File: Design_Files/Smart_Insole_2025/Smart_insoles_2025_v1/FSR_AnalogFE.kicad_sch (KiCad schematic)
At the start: 33 parts, among them J1 Conn_01x20, U8 MCP6004-I_ST, U9 MCP6004-I_ST

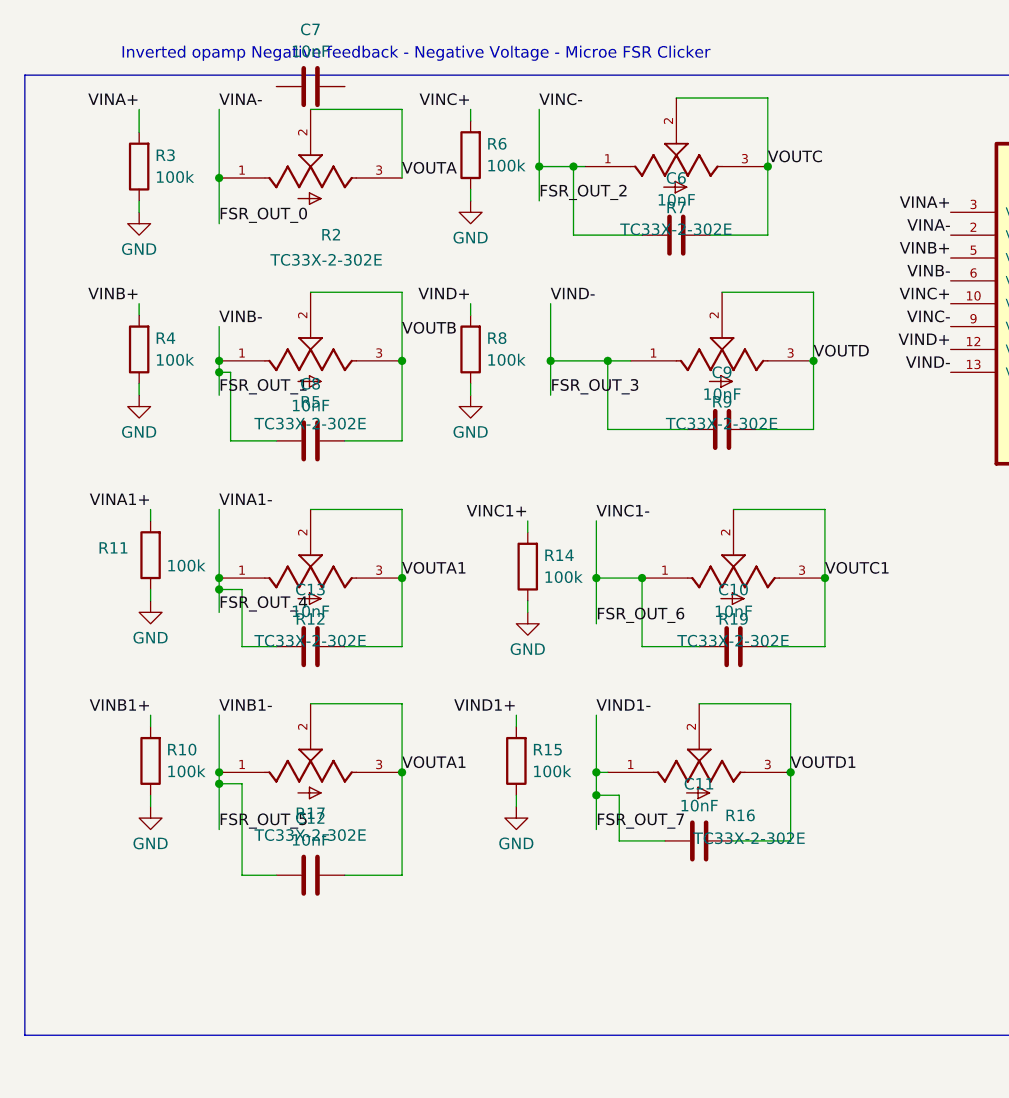
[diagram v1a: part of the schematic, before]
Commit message: Added battery connector footprint. Grouping componnets in PcbNew
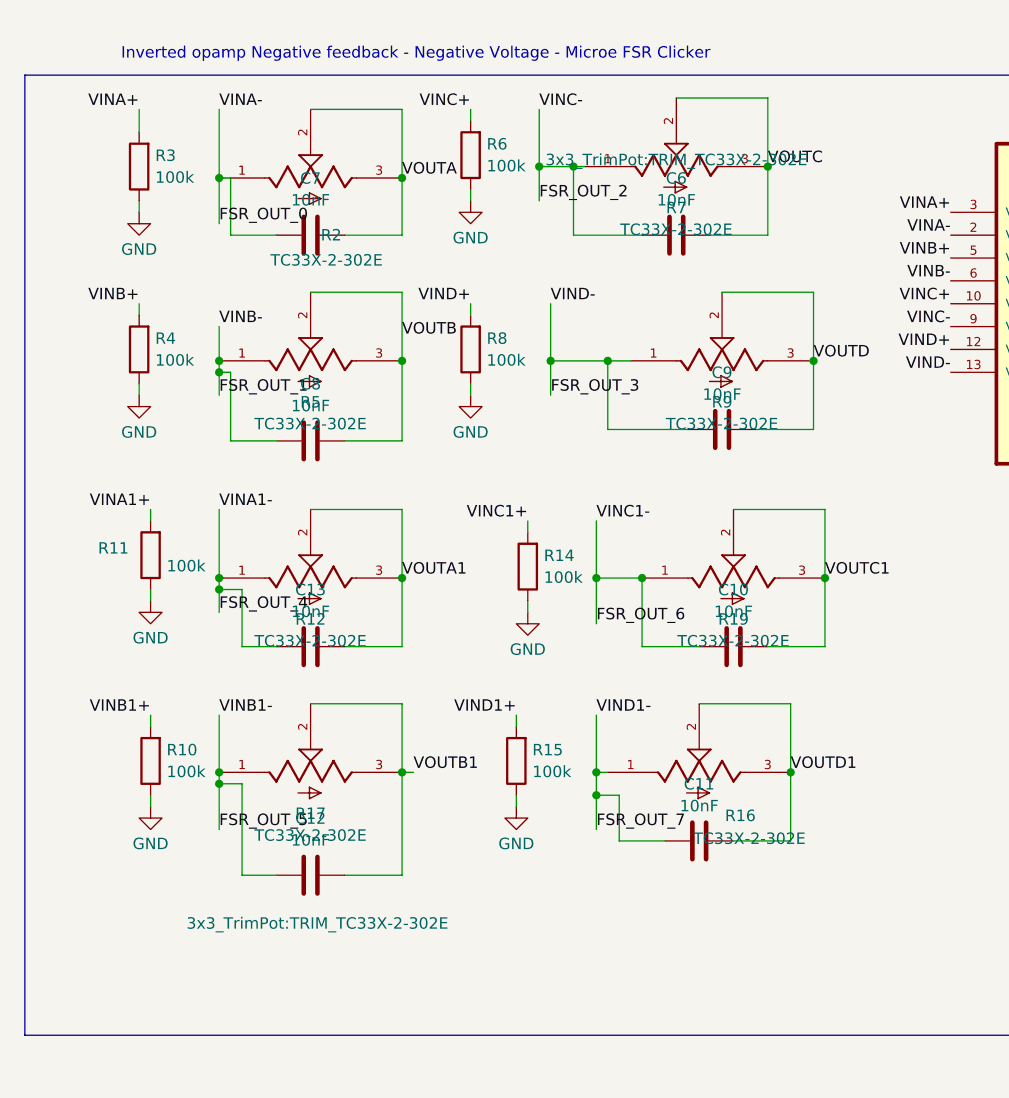
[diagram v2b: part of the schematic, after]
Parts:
- R12, R16, R17, R19, R2, R5, R7, R9: footprint TC33X-2-302E:TRIM_TC33X-2-302E -> 3x3_TrimPot:TRIM_TC33X-2-302E
- U9: footprint MCP6004-I_ST:SOP65P640X120-14N -> MCP6004_I_ST:SOP65P640X120-14N
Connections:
- net FSR_OUT_0: now also C7.1
- net VOUTA: now also C7.2
- net VOUTA1: no longer C12.2, R17.2, R17.3
- net VOUTB1: now also C12.2, R17.2, R17.3
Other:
- moved on the sheet: C7
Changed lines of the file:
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@@
 	)
 	(junction
+		(at 67.31 30.48)
+		(diameter 0)
+		(color 0 0 0 0)
+	)
+	(junction
 		(at 88.9 96.52)
 		(diameter 0)
@@
 	(wire
 		(pts
+			(xy 48.26 30.48) (xy 46.99 30.48)
+		)
+		(stroke
+			(width 0)
+			(type default)
+		)
+	)
+	(wire
+		(pts
 			(xy 86.36 29.21) (xy 87.63 29.21)
 		)
@@
 	(wire
 		(pts
+			(xy 60.96 36.83) (xy 67.31 36.83)
+		)
+		(stroke
+			(width 0)
+			(type default)
+		)
+	)
+	(wire
+		(pts
 			(xy 181.61 29.21) (xy 163.83 29.21)
 		)
@@
 	(wire
 		(pts
+			(xy 68.58 96.52) (xy 67.31 96.52)
+		)
+		(stroke
+			(width 0)
+			(type default)
+		)
+	)
+	(wire
+		(pts
 			(xy 86.36 36.83) (xy 93.98 36.83)
 		)
@@
 	(wire
 		(pts
+			(xy 53.34 36.83) (xy 48.26 36.83)
+		)
+		(stroke
+			(width 0)
+			(type default)
+		)
+	)
+	(wire
+		(pts
 			(xy 83.82 44.45) (xy 83.82 50.8)
 		)
@@
 	(wire
 		(pts
+			(xy 67.31 36.83) (xy 67.31 30.48)
+		)
+		(stroke
+			(width 0)
+			(type default)
+		)
+	)
+	(wire
+		(pts
 			(xy 67.31 88.9) (xy 67.31 96.52)
 		)
@@
 	(wire
 		(pts
+			(xy 48.26 36.83) (xy 48.26 30.48)
+		)
+		(stroke
+			(width 0)
+			(type default)
+		)
+	)
+	(wire
+		(pts
 			(xy 83.82 50.8) (xy 83.82 54.61)
 		)
@@
 		)
 	)
-	(label "VOUTA1"
-		(at 67.31 96.52 0)
+	(label "VOUTB1"
+		(at 68.58 96.52 0)
 		(fields_autoplaced yes)
 		(effects
@@
 			)
 		)
-		(property "Footprint" "TC33X-2-302E:TRIM_TC33X-2-302E"
+		(property "Footprint" "3x3_TrimPot:TRIM_TC33X-2-302E"
 			(at 97.79 29.21 0)
 			(effects
@@
 				)
 				(justify bottom)
-				(hide yes)
 			)
 		)
@@
 			)
 		)
-		(property "Footprint" "TC33X-2-302E:TRIM_TC33X-2-302E"
+		(property "Footprint" "3x3_TrimPot:TRIM_TC33X-2-302E"
 			(at 57.15 74.93 0)
 			(effects
@@
 	(symbol
 		(lib_id "Device:C")
-		(at 57.15 20.32 90)
+		(at 57.15 36.83 90)
 		(unit 1)
 		(exclude_from_sim no)
@@
 		(fields_autoplaced yes)
 		(property "Reference" "C7"
-			(at 57.15 14.0165 90)
+			(at 57.15 30.5265 90)
 			(effects
 				(font
@@
 		)
 		(property "Value" "10nF"
-			(at 57.15 16.4408 90)
+			(at 57.15 32.9508 90)
 			(effects
 				(font
@@
 		)
 		(property "Footprint" "Capacitor_SMD:C_0603_1608Metric_Pad1.08x0.95mm_HandSolder"
-			(at 60.96 19.3548 0)
+			(at 60.96 35.8648 0)
 			(effects
 				(font
@@
 		)
 		(property "Datasheet" "~"
-			(at 57.15 20.32 0)
+			(at 57.15 36.83 0)
 			(effects
 				(font
@@
 		)
 		(property "Description" "Unpolarized capacitor"
-			(at 57.15 20.32 0)
+			(at 57.15 36.83 0)
 			(effects
 				(font
@@
 			)
 		)
-		(property "Footprint" "TC33X-2-302E:TRIM_TC33X-2-302E"
+		(property "Footprint" "3x3_TrimPot:TRIM_TC33X-2-302E"
 			(at 100.33 96.52 0)
 			(effects
@@
 			)
 		)
-		(property "Footprint" "MCP6004-I_ST:SOP65P640X120-14N"
+		(property "Footprint" "MCP6004_I_ST:SOP65P640X120-14N"
 			(at 233.68 44.45 0)
 			(effects
@@
 			)
 		)
-		(property "Footprint" "TC33X-2-302E:TRIM_TC33X-2-302E"
+		(property "Footprint" "3x3_TrimPot:TRIM_TC33X-2-302E"
 			(at 102.87 50.8 0)
 			(effects
@@
 			)
 		)
-		(property "Footprint" "TC33X-2-302E:TRIM_TC33X-2-302E"
+		(property "Footprint" "3x3_TrimPot:TRIM_TC33X-2-302E"
 			(at 57.15 30.48 0)
 			(effects
@@
 			)
 		)
-		(property "Footprint" "TC33X-2-302E:TRIM_TC33X-2-302E"
+		(property "Footprint" "3x3_TrimPot:TRIM_TC33X-2-302E"
 			(at 57.15 50.8 0)
 			(effects
@@
 		(on_board yes)
 		(dnp no)
-		(fields_autoplaced yes)
 		(property "Reference" "R17"
 			(at 57.15 101.1103 0)
@@
 			)
 		)
-		(property "Footprint" "TC33X-2-302E:TRIM_TC33X-2-302E"
-			(at 57.15 96.52 0)
+		(property "Footprint" "3x3_TrimPot:TRIM_TC33X-2-302E"
+			(at 57.912 114.046 0)
 			(effects
 				(font
@@
 				)
 				(justify bottom)
-				(hide yes)
 			)
 		)
@@
 			)
 		)
-		(property "Footprint" "TC33X-2-302E:TRIM_TC33X-2-302E"
+		(property "Footprint" "3x3_TrimPot:TRIM_TC33X-2-302E"
 			(at 104.14 74.93 0)
 			(effects

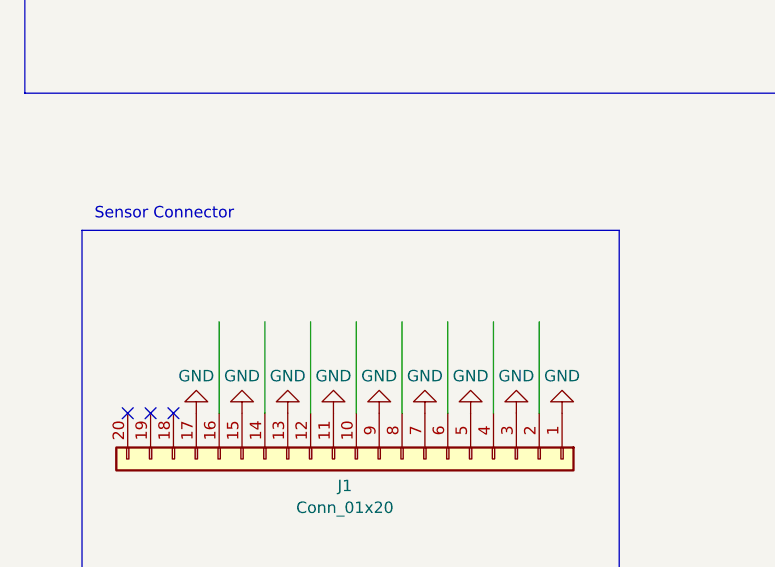
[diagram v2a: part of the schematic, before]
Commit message: PCBnew:Moving placed components. Fixed REF of mcp component
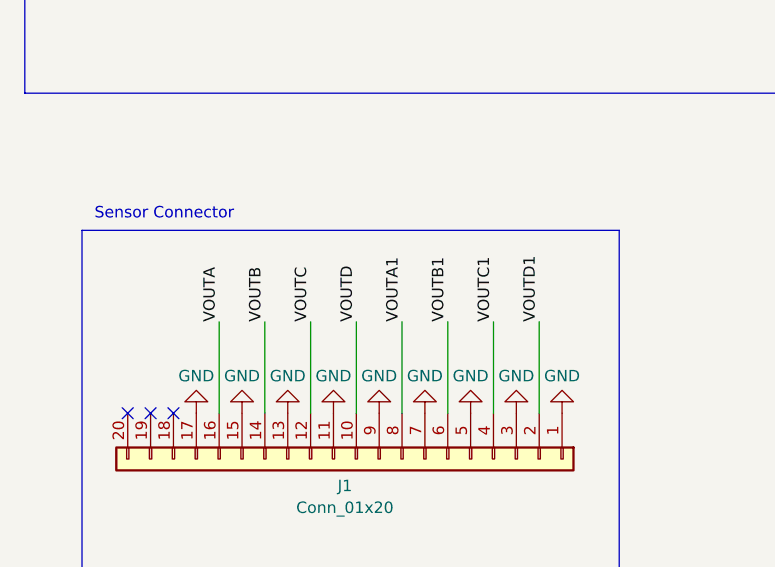
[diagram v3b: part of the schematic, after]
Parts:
- U8, U9: footprint MCP6004_I_ST:SOP65P640X120-14N -> MCP6004_I_ST:custom
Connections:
- net VOUTA: now also J1.16 (Pin_16)
- net VOUTA1: now also J1.8 (Pin_8)
- net VOUTB: now also J1.14 (Pin_14)
- net VOUTB1: now also J1.6 (Pin_6)
- net VOUTC: now also J1.12 (Pin_12)
- net VOUTC1: now also J1.4 (Pin_4)
- net VOUTD: now also J1.10 (Pin_10)
- net VOUTD1: now also J1.2 (Pin_2)
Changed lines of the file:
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@@
 	(wire
 		(pts
-			(xy 72.39 151.13) (xy 72.39 161.29)
-		)
-		(stroke
-			(width 0)
-			(type default)
-		)
-	)
-	(wire
-		(pts
 			(xy 86.36 36.83) (xy 86.36 29.21)
 		)
@@
 	(wire
 		(pts
+			(xy 72.39 151.13) (xy 72.39 161.29)
+		)
+		(stroke
+			(width 0)
+			(type default)
+		)
+	)
+	(wire
+		(pts
 			(xy 39.37 99.06) (xy 39.37 100.33)
 		)
@@
 		)
 	)
+	(label "VOUTA"
+		(at 46.99 151.13 90)
+		(fields_autoplaced yes)
+		(effects
+			(font
+				(size 1.27 1.27)
+			)
+			(justify left bottom)
+		)
+	)
 	(label "FSR_OUT_0"
 		(at 46.99 35.56 0)
@@
 		)
 	)
+	(label "VOUTD"
+		(at 62.23 151.13 90)
+		(fields_autoplaced yes)
+		(effects
+			(font
+				(size 1.27 1.27)
+			)
+			(justify left bottom)
+		)
+	)
 	(label "VIND+"
 		(at 74.93 44.45 180)
@@
 		)
 	)
+	(label "VOUTA1"
+		(at 67.31 151.13 90)
+		(fields_autoplaced yes)
+		(effects
+			(font
+				(size 1.27 1.27)
+			)
+			(justify left bottom)
+		)
+	)
 	(label "VINC1+"
 		(at 81.28 68.58 180)
@@
 		)
 	)
+	(label "VOUTB1"
+		(at 72.39 151.13 90)
+		(fields_autoplaced yes)
+		(effects
+			(font
+				(size 1.27 1.27)
+			)
+			(justify left bottom)
+		)
+	)
 	(label "VOUTA"
 		(at 67.31 30.48 0)
@@
 		)
 	)
+	(label "VOUTC"
+		(at 57.15 151.13 90)
+		(fields_autoplaced yes)
+		(effects
+			(font
+				(size 1.27 1.27)
+			)
+			(justify left bottom)
+		)
+	)
 	(label "VINB-"
 		(at 46.99 46.99 0)
@@
 		)
 	)
+	(label "VOUTB"
+		(at 52.07 151.13 90)
+		(fields_autoplaced yes)
+		(effects
+			(font
+				(size 1.27 1.27)
+			)
+			(justify left bottom)
+		)
+	)
 	(label "VINA-"
 		(at 46.99 22.86 0)
@@
 		)
 	)
+	(label "VOUTD1"
+		(at 82.55 151.13 90)
+		(fields_autoplaced yes)
+		(effects
+			(font
+				(size 1.27 1.27)
+			)
+			(justify left bottom)
+		)
+	)
 	(label "VINB1-"
 		(at 46.99 90.17 0)
@@
 		)
 	)
+	(label "VOUTC1"
+		(at 77.47 151.13 90)
+		(fields_autoplaced yes)
+		(effects
+			(font
+				(size 1.27 1.27)
+			)
+			(justify left bottom)
+		)
+	)
 	(label "VOUTB1"
 		(at 68.58 96.52 0)
@@
 			)
 		)
-		(property "Footprint" "MCP6004_I_ST:SOP65P640X120-14N"
+		(property "Footprint" "MCP6004_I_ST:custom"
 			(at 146.05 44.45 0)
 			(effects
@@
 			)
 		)
+		(property "MPN" ""
+			(at 146.05 44.45 0)
+			(effects
+				(font
+					(size 1.27 1.27)
+				)
+			)
+		)
+		(property "Manufacturer" ""
+			(at 146.05 44.45 0)
+			(effects
+				(font
+					(size 1.27 1.27)
+				)
+			)
+		)
+		(property "3D model" ""
+			(at 146.05 44.45 0)
+			(effects
+				(font
+					(size 1.27 1.27)
+				)
+			)
+		)
+		(property "Notes" ""
+			(at 146.05 44.45 0)
+			(effects
+				(font
+					(size 1.27 1.27)
+				)
+			)
+		)
+		(property "LCSC Part #" ""
+			(at 146.05 44.45 0)
+			(effects
+				(font
+					(size 1.27 1.27)
+				)
+			)
+		)
+		(property "LCSC MPN" ""
+			(at 146.05 44.45 0)
+			(effects
+				(font
+					(size 1.27 1.27)
+				)
+			)
+		)
+		(property "LCSC Manufacturer" ""
+			(at 146.05 44.45 0)
+			(effects
+				(font
+					(size 1.27 1.27)
+				)
+			)
+		)
 		(pin "1"
 		)
@@
 			)
 		)
-		(property "Footprint" "MCP6004_I_ST:SOP65P640X120-14N"
+		(property "Footprint" "MCP6004_I_ST:custom"
 			(at 233.68 44.45 0)
 			(effects
@@
 			)
 		)
+		(property "MPN" ""
+			(at 233.68 44.45 0)
+			(effects
+				(font
+					(size 1.27 1.27)
+				)
+			)
+		)
+		(property "Manufacturer" ""
+			(at 233.68 44.45 0)
+			(effects
+				(font
+					(size 1.27 1.27)
+				)
+			)
+		)
+		(property "3D model" ""
+			(at 233.68 44.45 0)
+			(effects
+				(font
+					(size 1.27 1.27)
+				)
+			)
+		)
+		(property "Notes" ""
+			(at 233.68 44.45 0)
+			(effects
+				(font
+					(size 1.27 1.27)
+				)
+			)
+		)
+		(property "LCSC Part #" ""
+			(at 233.68 44.45 0)
+			(effects
+				(font
+					(size 1.27 1.27)
+				)
+			)
+		)
+		(property "LCSC MPN" ""
+			(at 233.68 44.45 0)
+			(effects
+				(font
+					(size 1.27 1.27)
+				)
+			)
+		)
+		(property "LCSC Manufacturer" ""
+			(at 233.68 44.45 0)
+			(effects
+				(font
+					(size 1.27 1.27)
+				)
+			)
+		)

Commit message: PCB new moving things around
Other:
- moved on the sheet: C17
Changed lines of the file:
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@@
 	)
 	(junction
-		(at 264.16 27.94)
+		(at 264.16 29.21)
 		(diameter 0)
 		(color 0 0 0 0)
@@
 	(wire
 		(pts
-			(xy 251.46 29.21) (xy 251.46 27.94)
-		)
-		(stroke
-			(width 0)
-			(type default)
-		)
-	)
-	(wire
-		(pts
 			(xy 67.31 151.13) (xy 67.31 161.29)
 		)
@@
 	(wire
 		(pts
-			(xy 251.46 27.94) (xy 264.16 27.94)
+			(xy 251.46 29.21) (xy 264.16 29.21)
 		)
 		(stroke
@@
 	(symbol
 		(lib_id "power:VCC")
-		(at 264.16 27.94 0)
+		(at 264.16 29.21 0)
 		(unit 1)
 		(exclude_from_sim no)
@@
 		(fields_autoplaced yes)
 		(property "Reference" "#PWR045"
-			(at 264.16 31.75 0)
+			(at 264.16 33.02 0)
 			(effects
 				(font
@@
 		)
 		(property "Value" "VCC"
-			(at 264.16 23.8069 0)
+			(at 264.16 25.0769 0)
 			(effects
 				(font
@@
 		)
 		(property "Footprint" ""
-			(at 264.16 27.94 0)
+			(at 264.16 29.21 0)
 			(effects
 				(font
@@
 		)
 		(property "Datasheet" ""
-			(at 264.16 27.94 0)
+			(at 264.16 29.21 0)
 			(effects
 				(font
@@
 		)
 		(property "Description" "Power symbol creates a global label with name \"VCC\""
-			(at 264.16 27.94 0)
+			(at 264.16 29.21 0)
 			(effects
 				(font
@@
 		(on_board yes)
 		(dnp no)
-		(fields_autoplaced yes)
 		(property "Reference" "R7"
 			(at 97.79 33.8003 0)
@@
 		)
 		(property "Footprint" "3x3_TrimPot:TRIM_TC33X-2-302E"
-			(at 97.79 29.21 0)
+			(at 99.568 40.64 0)
 			(effects
 				(font
@@
 				)
 				(justify bottom)
+				(hide yes)
 			)
 		)
@@
 	(symbol
 		(lib_id "Device:C")
-		(at 264.16 31.75 0)
+		(at 264.16 33.02 0)
 		(unit 1)
 		(exclude_from_sim no)
@@
 		(fields_autoplaced yes)
 		(property "Reference" "C17"
-			(at 267.081 30.5378 0)
+			(at 267.081 31.8078 0)
 			(effects
 				(font
@@
 		)
 		(property "Value" "1uF"
-			(at 267.081 32.9621 0)
+			(at 267.081 34.2321 0)
 			(effects
 				(font
@@
 		)
 		(property "Footprint" "Capacitor_SMD:C_0603_1608Metric_Pad1.08x0.95mm_HandSolder"
-			(at 265.1252 35.56 0)
+			(at 265.1252 36.83 0)
 			(effects
 				(font
@@
 		)
 		(property "Datasheet" "~"
-			(at 264.16 31.75 0)
+			(at 264.16 33.02 0)
 			(effects
 				(font
@@
 		)
 		(property "Description" "Unpolarized capacitor"
-			(at 264.16 31.75 0)
+			(at 264.16 33.02 0)
 			(effects
 				(font
@@
 	(symbol
 		(lib_id "power:GND")
-		(at 264.16 35.56 0)
+		(at 264.16 36.83 0)
 		(unit 1)
 		(exclude_from_sim no)
@@
 		(fields_autoplaced yes)
 		(property "Reference" "#PWR044"
-			(at 264.16 41.91 0)
+			(at 264.16 43.18 0)
 			(effects
 				(font
@@
 		)
 		(property "Value" "GND"
-			(at 264.16 39.6931 0)
+			(at 264.16 40.9631 0)
 			(effects
 				(font
@@
 		)
 		(property "Footprint" ""
-			(at 264.16 35.56 0)
+			(at 264.16 36.83 0)
 			(effects
 				(font
@@
 		)
 		(property "Datasheet" ""
-			(at 264.16 35.56 0)
+			(at 264.16 36.83 0)
 			(effects
 				(font
@@
 		)
 		(property "Description" "Power symbol creates a global label with name \"GND\" , ground"
-			(at 264.16 35.56 0)
+			(at 264.16 36.83 0)
 			(effects
 				(font

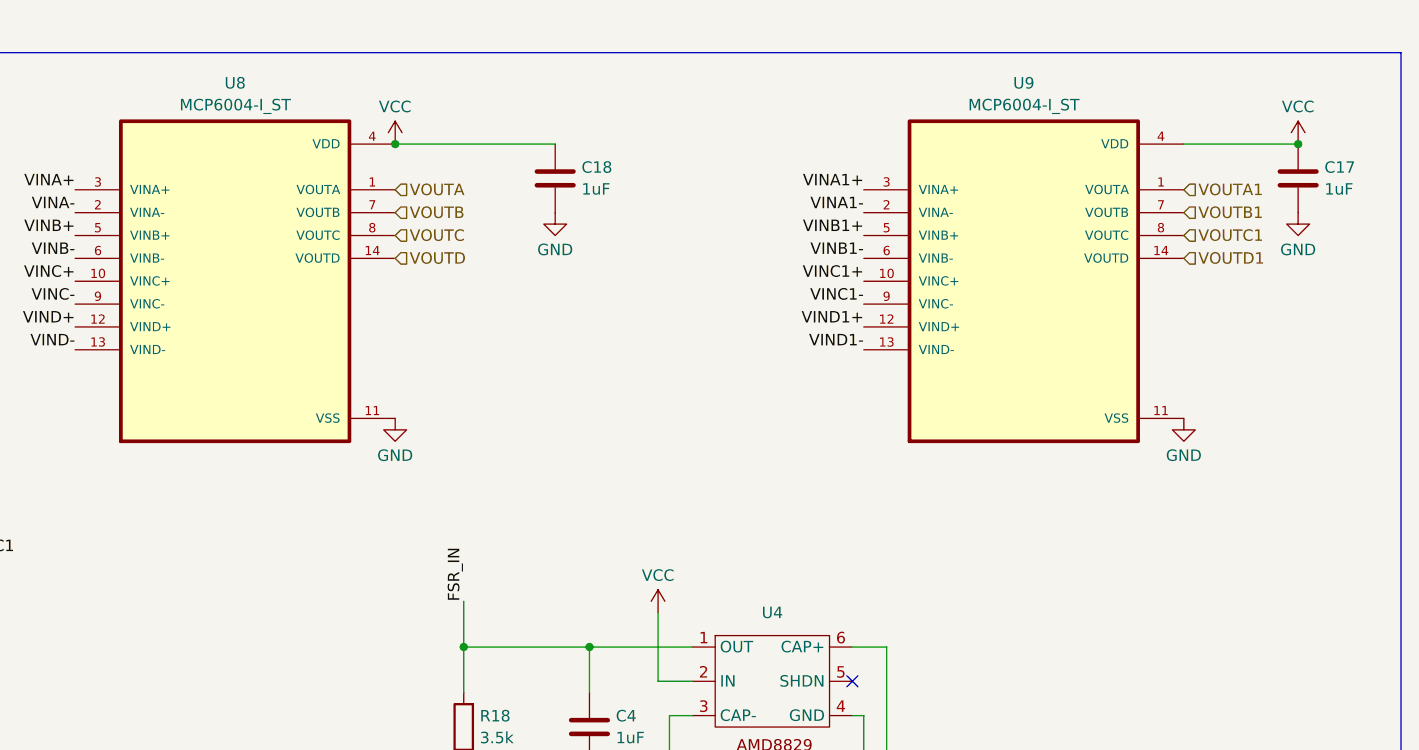
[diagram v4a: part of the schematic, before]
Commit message: SCH: Advances in Battery circuit. Added External_Periph sheet
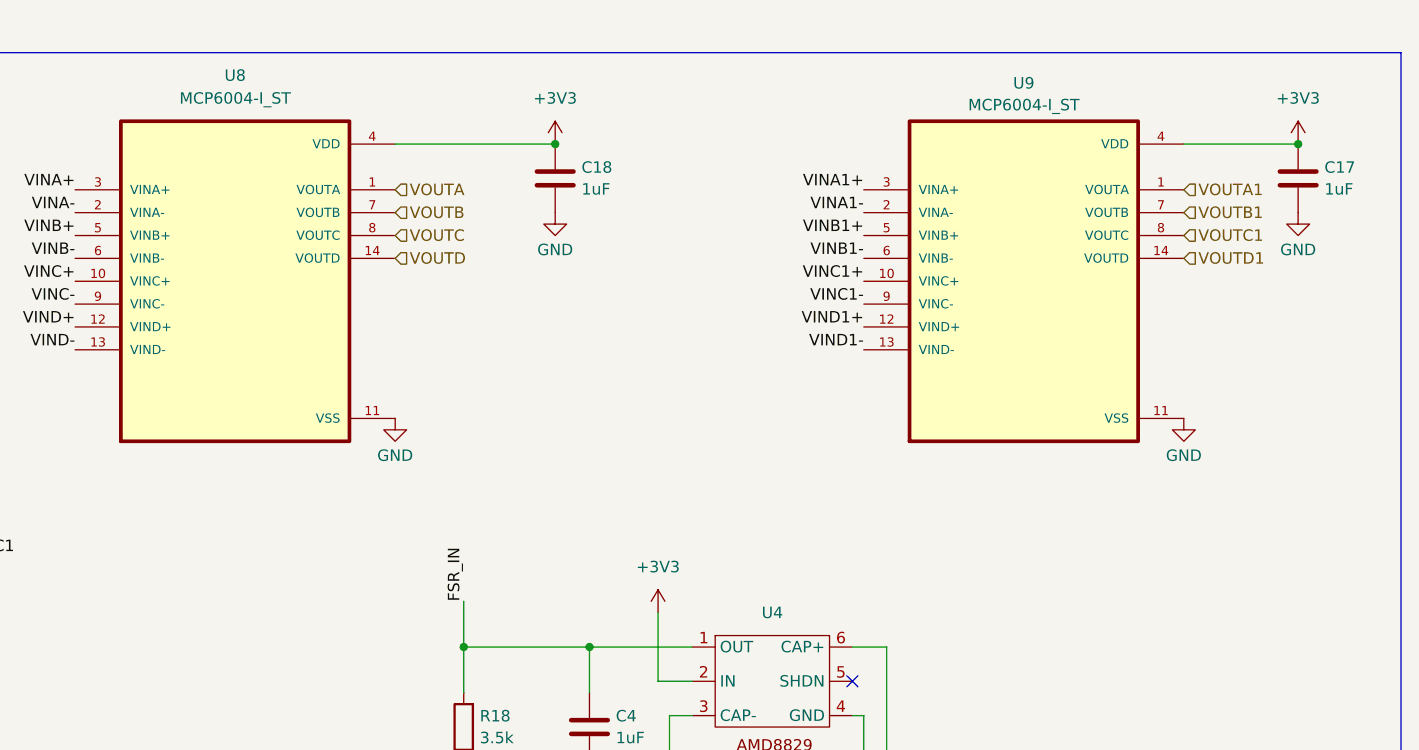
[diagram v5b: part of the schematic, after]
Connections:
- net VCC renamed +3V3
